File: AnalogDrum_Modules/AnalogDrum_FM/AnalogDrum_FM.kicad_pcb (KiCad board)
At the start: 2 copper layers, 100.3 x 160 mm, 144 parts, among them J101 Conn_01x05_Male, Q301 2N3904, Q302 2N3904, Q303 2N3904, Q501 2N3904, Q502 2N3904, Q503 2N3904, SW101 SW_SPDT, SW102 SW_SPDT, SW401 SW_DPDT_x2, SW402 SW_DPDT_x2, U201 NE5532, U202 LM13700, U203 NE5532, U301 TL074, U302 LM358, U401 TL074, U501 TL074, U502 LM358

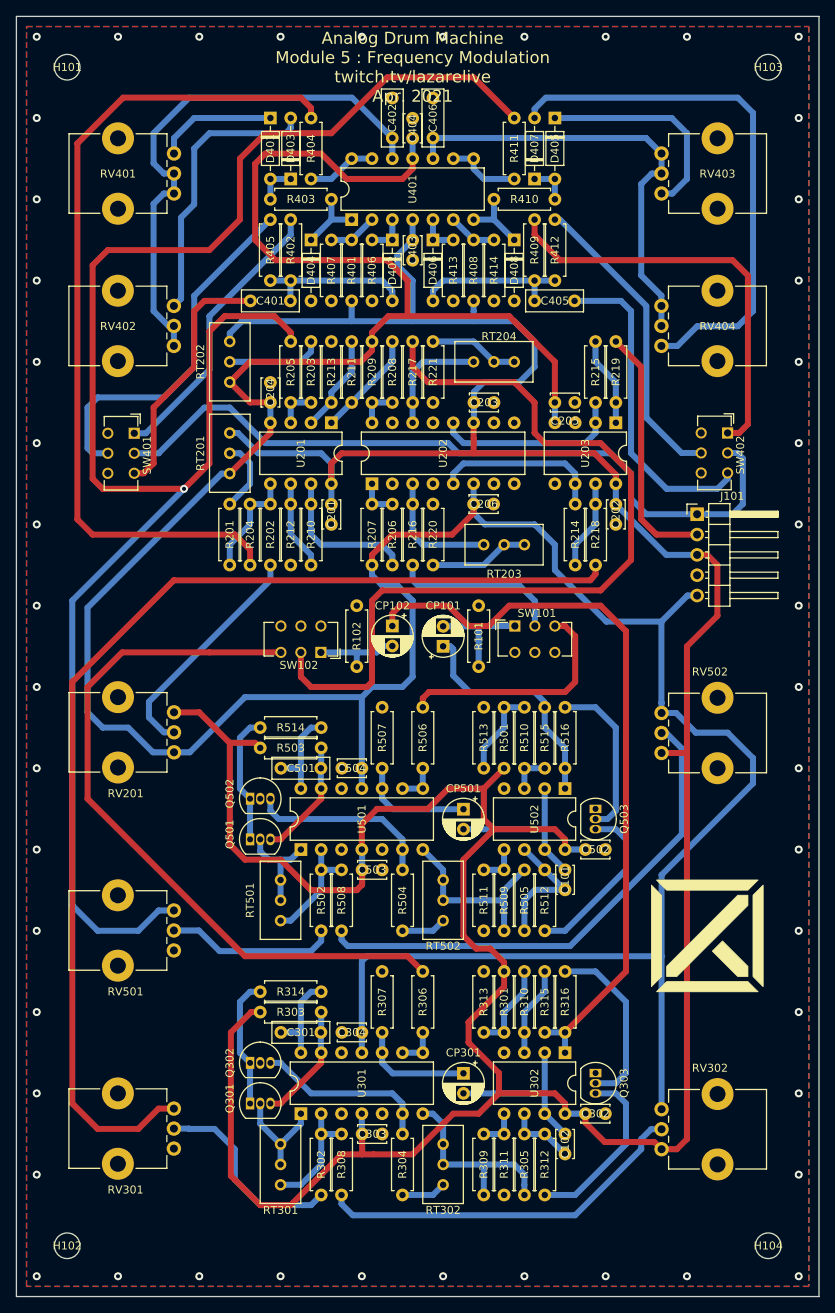
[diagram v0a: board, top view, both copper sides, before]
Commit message: Version 0.1.1
Corrections mineures :
- Vérification des potentiomètres
- Passage des connecteurs de carte e n JST
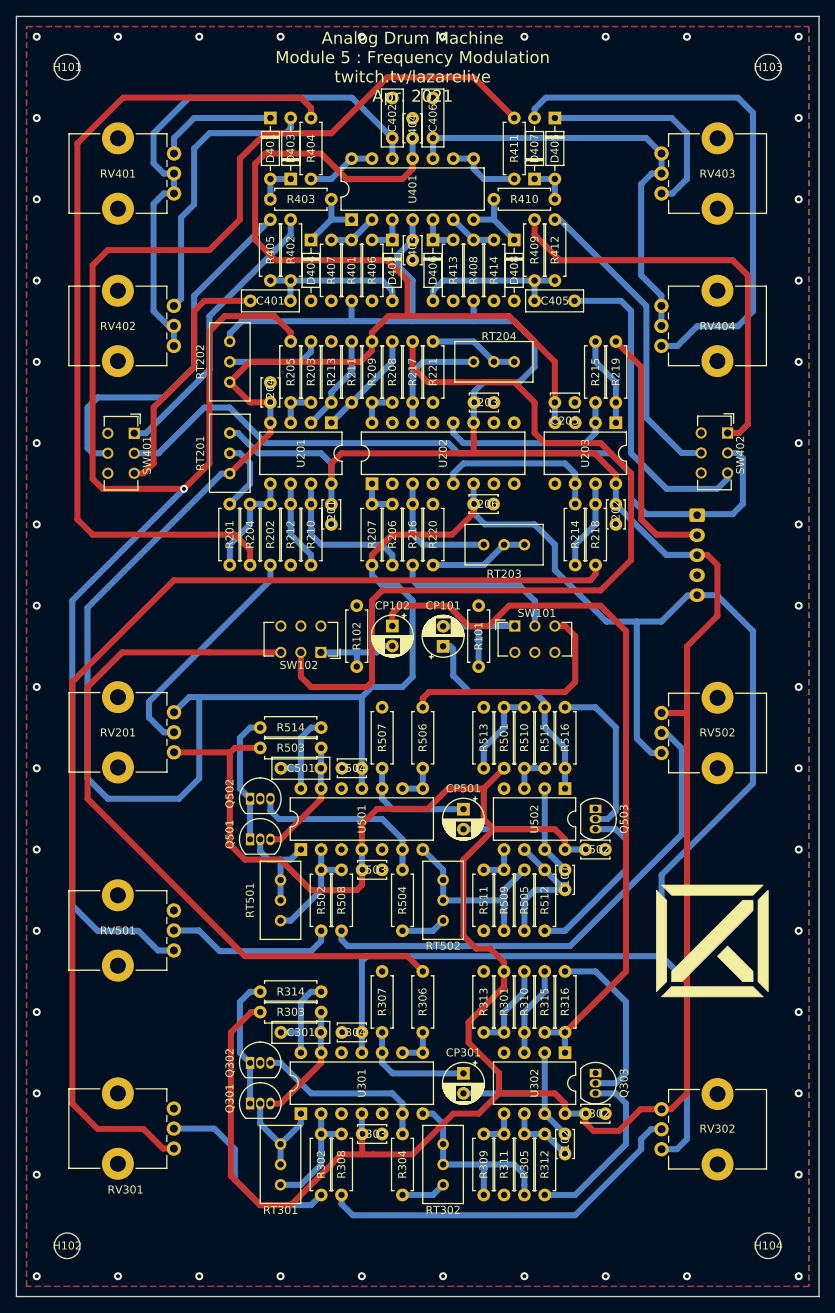
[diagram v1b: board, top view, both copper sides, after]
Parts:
- J101: footprint Connector_PinHeader_2.54mm:PinHeader_1x05_P2.54mm_Horizontal -> Connector_JST:JST_EH_B5B-EH-A_1x05_P2.50mm_Vertical; moved to B.Cu
- moved REF** 0.90 mm to (145.4, 134.6)
- moved J101 0.12 mm to (143.5, 81.4), turned to 270 degrees
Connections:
- RV201 pad 1: +12V -> -12V
- RV201 pad 3: -12V -> +12V
- RV301 pad 1: /VCO_Carrier/MOD_IN -> GNDA
- RV301 pad 3: GNDA -> /VCO_Carrier/MOD_IN
- RV302 pad 1: +12V -> -12V
- RV302 pad 3: -12V -> +12V
- RV501 pad 1: /EG/EGB_OUT -> GNDA
- RV501 pad 3: GNDA -> /EG/EGB_OUT
- RV502 pad 1: +12V -> -12V
- RV502 pad 3: -12V -> +12V
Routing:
- net -12V: track 427.2 -> 473.5 mm
- net +12V: track 464.8 -> 456.7 mm
